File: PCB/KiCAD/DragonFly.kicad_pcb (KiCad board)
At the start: 2 copper layers, 120 x 93 mm, 180 parts, among them CON1 AVR-ISP-6, CON2 BARREL_JACK, J1 USB_OTG, J2 JACK_TRS_3pins, J3 MIC, J4 Conn_Coaxial, J5 Conn_Coaxial, J6 Conn_01x10, J7 ANT, K1 TQ2-12VDC, P4 CONN_01X01, P5 CONN_01X01, P6 CONN_01X01, P7 CONN_01X01, Q1 MMBFJ310LT1G, Q10 MMBT4401LT1G, Q11 BFG591, Q3 SI2301-TP, Q4 SI2301-TP, Q5 MMBT2222A, Q6 MMBFJ310L, Q7 IRF610, T1 1_9, T2 1_4, T3 1_4, T4 Transformer_1P_2S, T5 Transformer_1P_2S, U1 NE5532, U10 LD1117S33TR, U11 NC7SB3157, U12 NC7SB3157, U13 L78L06_TO92, U2 ATMEGA8-16AU, U3 ADuM1201CR, U4 L78L06_TO92, U5 SA612, U6 FT232RL, U7 SI5351, U8 L78L06_TO92, U9 SA612, Y1 8Mhz, Y10 8Mhz, Y2 8Mhz, Y3 8Mhz, Y4 8Mhz, Y5 8Mhz, Y6 8Mhz, Y7 8Mhz, Y8 27Mhz, Y9 8Mhz

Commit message: denser layout
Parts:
- moved C7 20.6 mm to (134.0, 49.4), turned to 90 degrees
- moved C59 17.4 mm to (54.3, 24.1), turned to 180 degrees
- moved C3 15.6 mm to (128.5, 48.3), turned to 90 degrees
- moved C28 15.5 mm to (70.8, 24.6)
- moved R8 14.1 mm to (131.1, 48.3), turned to 270 degrees
- moved C2 11.4 mm to (150.7, 38.1)
- moved R3 11.4 mm to (152.8, 38.1)
- moved C71 10.6 mm to (137.2, 56.2), turned to 90 degrees
- moved RV2 9.62 mm to (59.9, 37.7)
- moved T4 8.95 mm to (144.1, 45.3)
- moved U5 8.93 mm to (70.2, 30.6), turned to 270 degrees
- moved T5 8.79 mm to (144.1, 50.4)
- moved C21 8.08 mm to (68.6, 37.0), turned to 270 degrees
- moved R40 7.23 mm to (131.3, 57.6)
- moved U11 6.66 mm to (141.2, 54.0)
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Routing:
- net Net-(C3-Pad1): track 0.00 -> 27.5 mm
- net Net-(C70-Pad1): track 0.00 -> 20.1 mm
- net IF_TX: track 18.4 -> 0.00 mm
- net Net-(T4-Pad4): track 0.00 -> 16.2 mm, vias 0 -> 1
- net Net-(D3-Pad1): track 15.4 -> 0.35 mm
- net Net-(C23-Pad1): track 0.00 -> 13.8 mm
- net Net-(T4-Pad6): track 0.00 -> 12.6 mm
- net Net-(C59-Pad2): track 0.00 -> 11.2 mm
- net Net-(Q10-Pad1): track 10.7 -> 0.14 mm
- net Net-(T4-Pad3): track 0.00 -> 9.61 mm
- net Net-(T4-Pad5): track 0.00 -> 9.41 mm
- net Net-(C6-Pad1): track 0.00 -> 9.27 mm
- net TX_12V: track 9.04 -> 0.00 mm
- net Net-(Q10-Pad2): track 7.47 -> 0.00 mm
- net Net-(R34-Pad1): track 0.00 -> 6.88 mm
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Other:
- board size 120 x 93 mm -> 120 x 89 mm

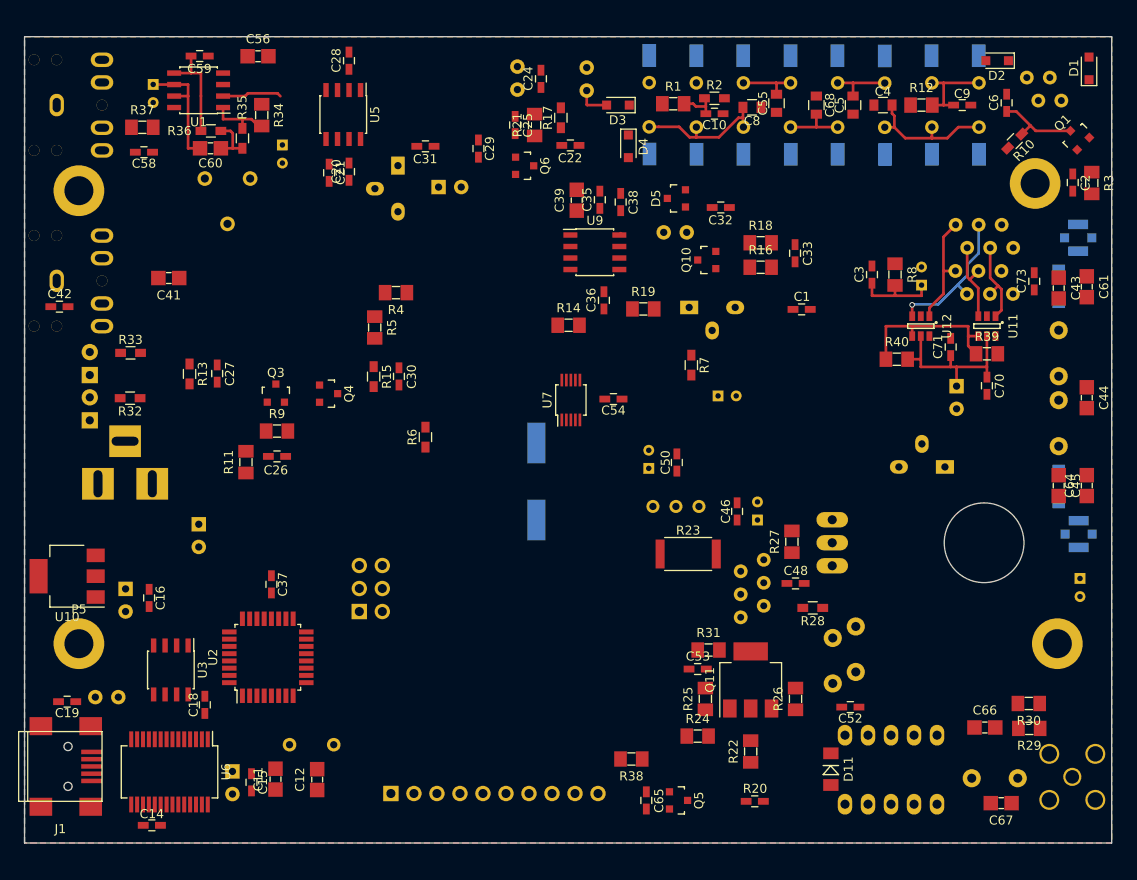
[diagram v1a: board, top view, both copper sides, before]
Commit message: add AGC circuit
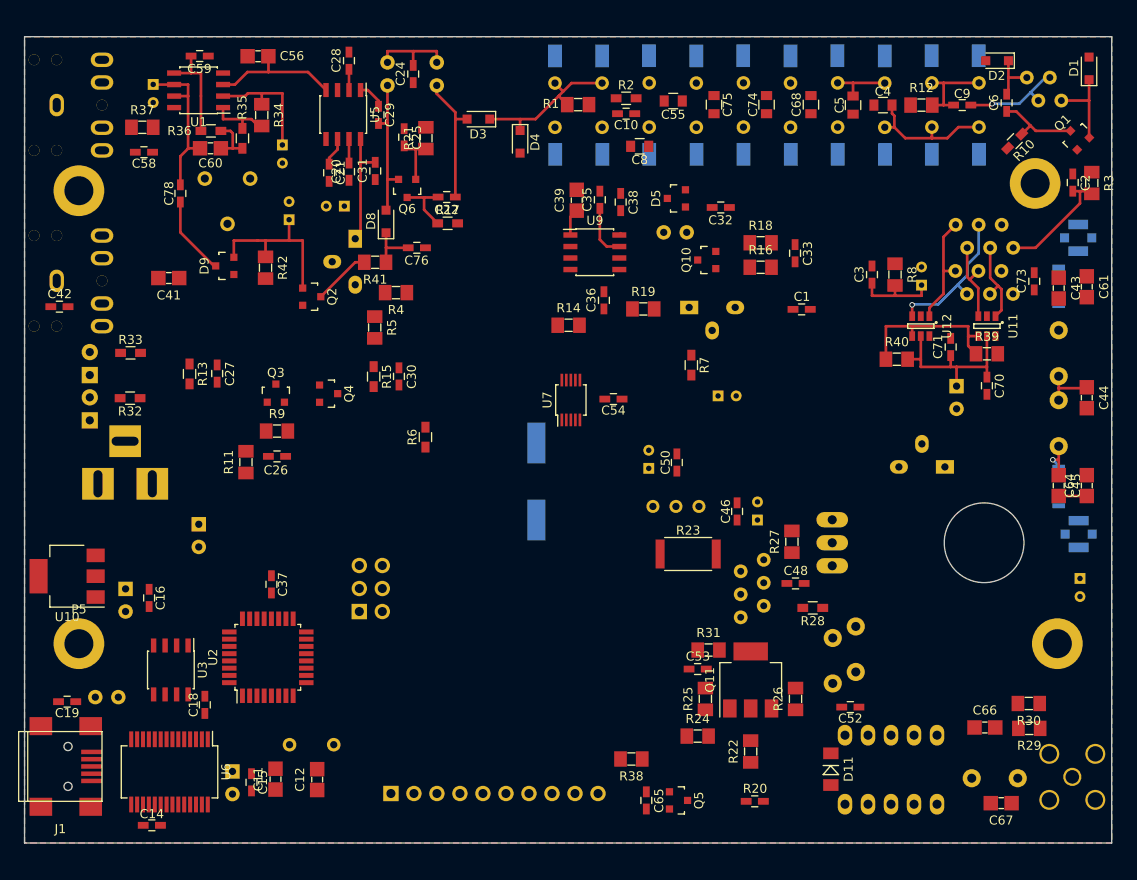
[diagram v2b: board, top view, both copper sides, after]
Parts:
- added C74: 62, Capacitors_SMD:C_0805, F.Cu at (116.9, 29.5)
- added C75: 62, Capacitors_SMD:C_0805, F.Cu at (111.1, 29.5)
- added C76: 100nF, DragonFly:C_0603_HandSoldering, F.Cu at (78.3, 45.3)
- added C77: 10µF, DragonFly:CP_Radial_D4.0mm_P2.00mm, B.Cu at (64.2, 42.2)
- added C78: 100nF, Capacitors_SMD:C_0603_HandSoldering, F.Cu at (52.2, 39.3)
- added D8: BAP50-03, DragonFly:D_SOD-323_HandSoldering, F.Cu at (74.9, 42.4)
- added D9: BAV99, DragonFly:SOT-23, F.Cu at (57.1, 47.3)
- added Q2: 2N7002, DragonFly:SOT-23, F.Cu at (66.7, 50.7)
- added R41: 330, DragonFly:R_1206_0603, F.Cu at (73.7, 46.9)
- added R42: 1M, DragonFly:R_1206_0603, F.Cu at (61.6, 47.5)
- added Y11: 8Mhz, DragonFly:Crystal_HC49-U_Vertical, B.Cu at (114.3, 27.1)
- added Y12: 8Mhz, DragonFly:Crystal_HC49-U_Vertical, B.Cu at (109.2, 32.0)
- C34: value 100µF -> 10µF; footprint DragonFly:CP_Radial_D6.3mm_P2.50mm -> DragonFly:CP_Radial_D4.0mm_P2.00mm
- moved R17 17.1 mm to (81.7, 42.6), turned to 0 degrees
- moved L1 16.6 mm to (80.5, 24.8)
- moved D3 15.5 mm to (85.1, 31.1)
- moved C22 14.8 mm to (81.6, 39.7)
- moved L3 14.3 mm to (75.1, 24.8)
- moved C24 14.1 mm to (77.9, 26.1)
- moved Q6 13.2 mm to (77.2, 38.8), turned to 180 degrees
- moved C8 13.1 mm to (102.9, 34.1)
- moved C25 12.3 mm to (76.9, 33.1)
- moved R21 12.1 mm to (79.3, 33.2)
- moved D4 12.0 mm to (89.7, 33.6)
- moved C29 11.6 mm to (74.1, 30.6)
- moved C55 11.4 mm to (106.6, 29.1), turned to 180 degrees
- moved C34 10.6 mm to (70.3, 40.7), turned to 180 degrees
- moved R1 10.5 mm to (96.1, 29.5)
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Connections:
- Y10 pad 2: Net-(C55-Pad2) -> Net-(C74-Pad2)
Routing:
- net Net-(C77-Pad1): track 0.00 -> 18.8 mm
- net Net-(D3-Pad1): track 0.35 -> 17.9 mm
- net Net-(C29-Pad2): track 0.00 -> 16.0 mm
- net Net-(C8-Pad2): track 15.0 -> 0.00 mm
- net Net-(C56-Pad2): track 0.00 -> 14.5 mm
- net IF: track 0.00 -> 13.0 mm
- net Net-(C31-Pad2): track 0.00 -> 12.9 mm
- net Net-(C9-Pad2): track 0.00 -> 11.2 mm, vias 0 -> 1
- net IF_RX: track 3.77 -> 14.5 mm
- net RX_12V: track 0.00 -> 9.49 mm
- net Net-(D1-Pad1): track 0.00 -> 9.46 mm
- net Net-(C78-Pad1): track 0.00 -> 8.78 mm
- net Net-(C57-Pad1): track 6.59 -> 13.6 mm
- net Net-(C22-Pad2): track 0.00 -> 6.91 mm
- net Net-(C68-Pad2): track 6.63 -> 0.00 mm
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
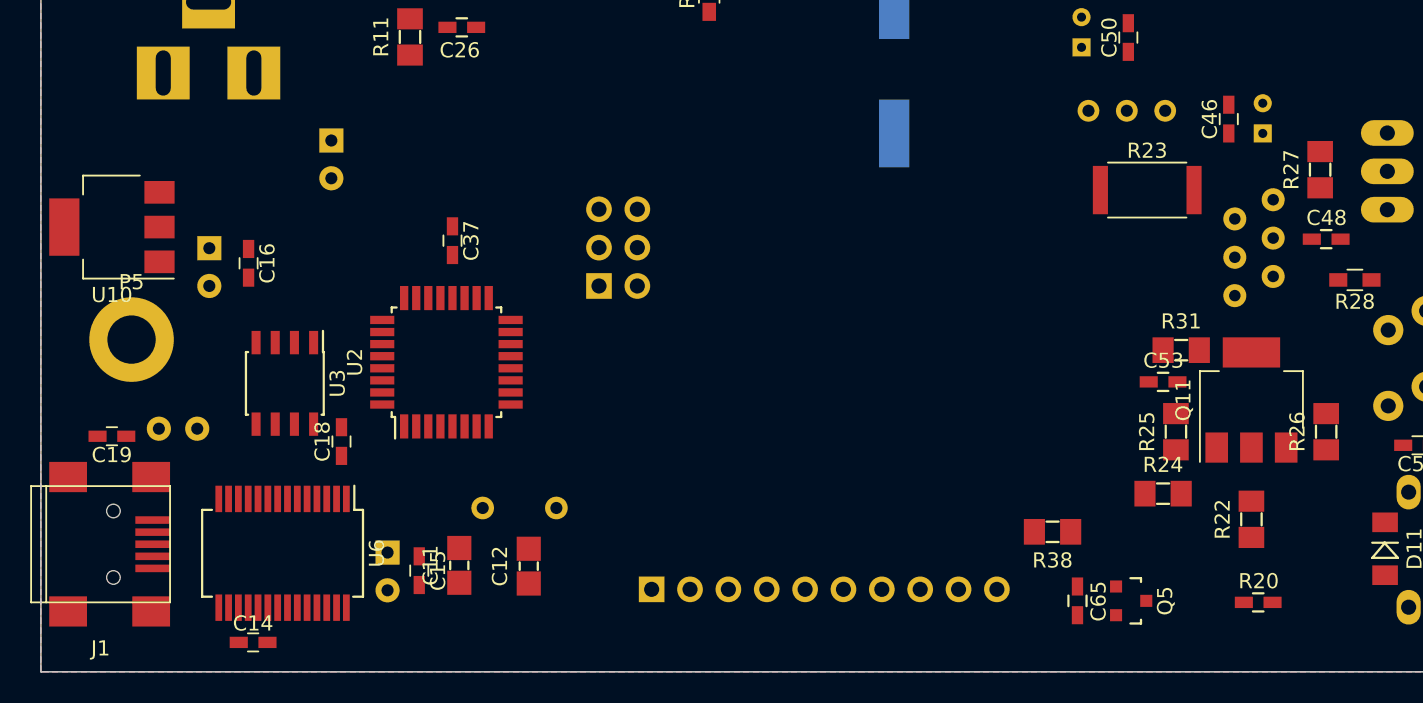
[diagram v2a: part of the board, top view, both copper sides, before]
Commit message: add FM24CL16,PCB progress
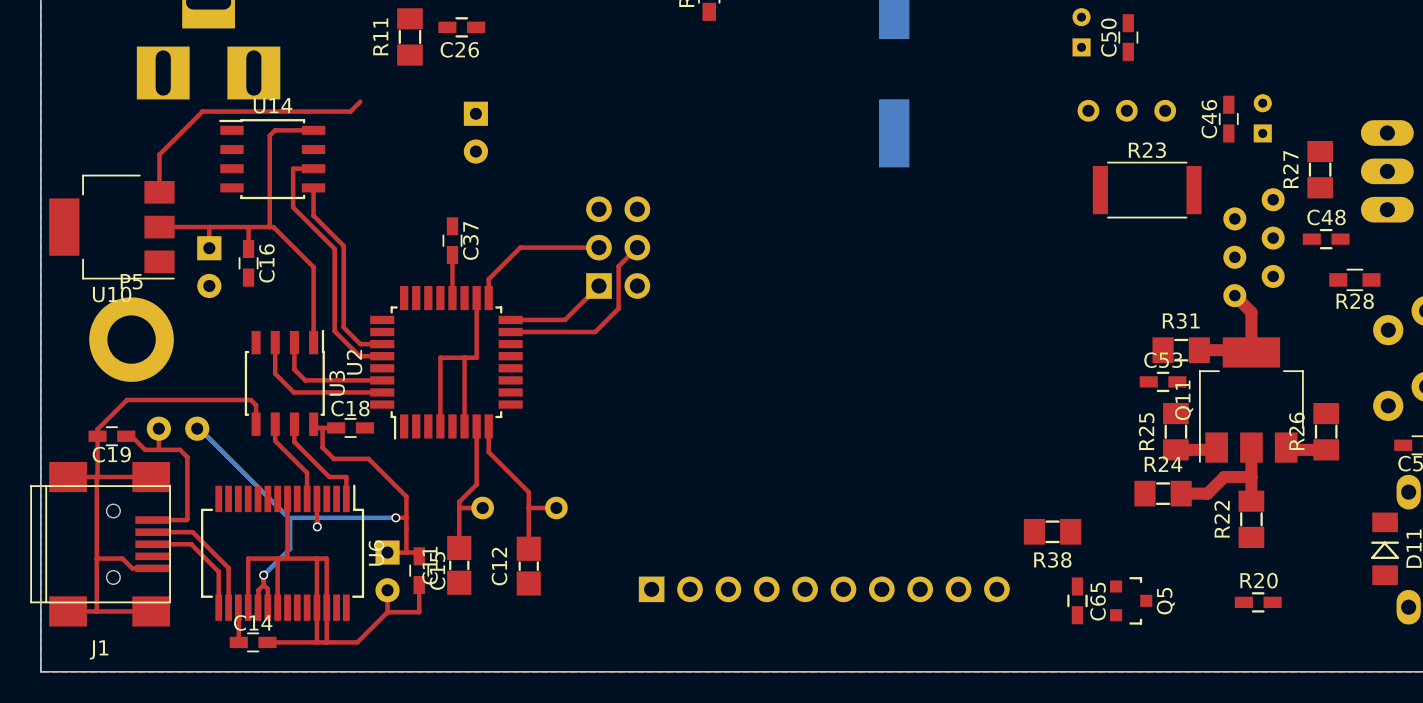
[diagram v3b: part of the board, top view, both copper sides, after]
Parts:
- added U14: FM24CL16, DragonFly:SOIC-8_3.9x4.9mm_Pitch1.27mm, F.Cu at (50.4, 77.0)
- moved C69 9.73 mm to (63.8, 74.0)
- moved C18 1.08 mm to (55.5, 94.8), turned to 0 degrees
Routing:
- net GNDD: track 0.00 -> 80.6 mm
- net +3V3: track 0.00 -> 43.7 mm
- net Net-(C13-Pad1): track 0.00 -> 43.1 mm, vias 0 -> 3
- net +12V: track 0.00 -> 17.2 mm
- net SCL: track 0.00 -> 17.1 mm
- net SDA: track 0.00 -> 13.1 mm
- net Net-(C19-Pad1): track 0.00 -> 12.5 mm
- net Net-(CON1-Pad4): track 0.00 -> 12.3 mm
- net Net-(C12-Pad2): track 0.00 -> 11.0 mm
- net Net-(C11-Pad2): track 0.00 -> 10.1 mm
- net Net-(U2-Pad31): track 0.00 -> 9.66 mm
- net Net-(CON1-Pad3): track 0.00 -> 9.42 mm
- net Net-(C53-Pad2): track 0.00 -> 8.66 mm
- net Net-(J1-Pad2): track 0.00 -> 8.63 mm
- net Net-(U2-Pad30): track 0.00 -> 7.90 mm
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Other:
- net class Default: trace_width 0.3 -> 0.8

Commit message: PCB v1.0
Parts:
- added C79: 100nF, DragonFly:C_1206_0603, F.Cu at (66.5, 80.2)
- added C80: 100nF, DragonFly:C_1206_0603, F.Cu at (56.6, 73.4)
- added L8: 4.7µH, DragonFly:Choke_CD54, B.Cu at (131.7, 78.2)
- added Q8: 2N7002, DragonFly:SOT-23, F.Cu at (61.7, 52.2)
- added R43: 3.3K, DragonFly:R_1206_0603, F.Cu at (57.2, 54.2)
- added R44: 56R, DragonFly:R_0603_HandSoldering, F.Cu at (85.6, 102.2)
- added R45: 56R, DragonFly:R_0603_HandSoldering, F.Cu at (88.1, 102.2)
- added R46: 56R, DragonFly:R_0603_HandSoldering, F.Cu at (90.7, 102.2)
- added R47: 56R, DragonFly:R_0603_HandSoldering, F.Cu at (93.2, 102.2)
- added R48: 56R, DragonFly:R_0603_HandSoldering, F.Cu at (95.8, 102.2)
- C10, C16, C37, C46, C50, C52, C54, C58, C78: footprint Capacitors_SMD:C_0603_HandSoldering -> DragonFly:C_1206_0603
- C20, C24, C25, C26, C27, C28, C3, C30, C31, C32, C33, C35, C38, C53, C70, C71, C76: footprint DragonFly:C_0603_HandSoldering -> DragonFly:C_1206_0603
- C29, C6, C9: value 100nF -> 10nF
- R13, R15, R17, R2, R28, R32, R33: footprint DragonFly:R_0603_HandSoldering -> DragonFly:R_1206_0603
- R20: footprint DragonFly:C_0603_HandSoldering -> DragonFly:R_1206_0603
- R6, R7: footprint Resistors_SMD:R_0603_HandSoldering -> DragonFly:R_1206_0603
- moved C27 82.0 mm to (134.8, 35.8), turned to 0 degrees
- moved C30 69.3 mm to (136.2, 24.6), turned to 0 degrees
- moved R7 61.0 mm to (71.5, 106.7), turned to 90 degrees
- moved R6 36.6 mm to (80.5, 102.8), turned to 180 degrees
- moved C51 30.9 mm to (121.9, 90.7), turned to 180 degrees
- moved C49 19.0 mm to (122.8, 71.0), turned to 0 degrees
- moved D1 17.8 mm to (139.7, 37.8), turned to 180 degrees
- moved U13 12.3 mm to (126.5, 62.5)
- moved C54 12.0 mm to (90.0, 68.6), turned to 90 degrees
- moved C69 11.8 mm to (53.9, 67.6), turned to 90 degrees
- moved R19 11.3 mm to (95.2, 59.9), turned to 270 degrees
- moved R2 11.0 mm to (93.7, 36.6), turned to 180 degrees
- moved C7 8.92 mm to (126.9, 54.9), turned to 180 degrees
- moved Y8 8.47 mm to (85.9, 77.4), turned to 0 degrees
- moved U7 8.39 mm to (94.2, 70.4)
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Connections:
- J6 pad 5: IO1 -> Net-(J6-Pad5)
- J6 pad 6: IO2 -> Net-(J6-Pad6)
- J6 pad 7: IO3 -> Net-(J6-Pad7)
- J6 pad 8: IO4 -> Net-(J6-Pad8)
- J6 pad 9: IO5 -> Net-(J6-Pad9)
- U14 pad 7: (no net) -> WP
- U2 pad 25: (no net) -> AGC_OFF
- U2 pad 26: (no net) -> WP
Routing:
- net +12V: track 17.2 -> 201.5 mm, vias 0 -> 1
- net RX_12V: track 9.49 -> 185.4 mm
- net TX_12V: track 0.00 -> 139.4 mm, vias 0 -> 4
- net +3V3: track 43.7 -> 164.9 mm, vias 0 -> 2
- net GND: track 0.00 -> 88.0 mm, vias 0 -> 21
- net SDA: track 13.1 -> 87.2 mm, vias 0 -> 2
- net SCL: track 17.1 -> 86.5 mm, vias 0 -> 4
- net TX_6V: track 0.21 -> 68.1 mm, vias 0 -> 2
- net Net-(C41-Pad1): track 0.00 -> 54.6 mm, vias 0 -> 2
- net Net-(C45-Pad2): track 3.10 -> 48.9 mm, vias 0 -> 1
- net TX_PA: track 0.00 -> 39.8 mm
- net AGC_OFF: track 0.00 -> 35.3 mm, vias 0 -> 2
- net IO5: track 0.00 -> 35.2 mm
- net IO4: track 0.00 -> 32.2 mm
- net Net-(C51-Pad1): track 0.00 -> 29.8 mm
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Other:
- net class Default: trace_width 0.8 -> 0.3

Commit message: PCB production
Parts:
- added E1: SPARK_GAP, DragonFly:Resistor_Vertical_RM5mm, B.Cu at (149.0, 96.0)
- moved R29 6.20 mm to (152.1, 98.4), turned to 0 degrees
- moved R30 3.03 mm to (144.5, 98.3)
- moved J4 0.74 mm to (151.9, 43.4), turned to 90 degrees
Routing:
- net GND: track 88.0 -> 456.2 mm, vias 21 -> 101
- net BPF: track 15.0 -> 17.4 mm
- net Net-(C67-Pad1): track 23.2 -> 25.4 mm
- net Net-(C6-Pad1): track 9.01 -> 8.31 mm
